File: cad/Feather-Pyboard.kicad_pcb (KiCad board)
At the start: 2 copper layers, 22.9 x 55.9 mm, 39 parts, among them P1 CONN_01X16, P2 CONN_01X02, P3 CONN_01X12, P4 USB_OTG, SW1 RST, U1 SPX3819, U2 MCP73811T-420I/OT, U3 STM32F411CEUx, U4 MicroSD_SPI_CD, Y1 32.768Hz, Y2 8MHz

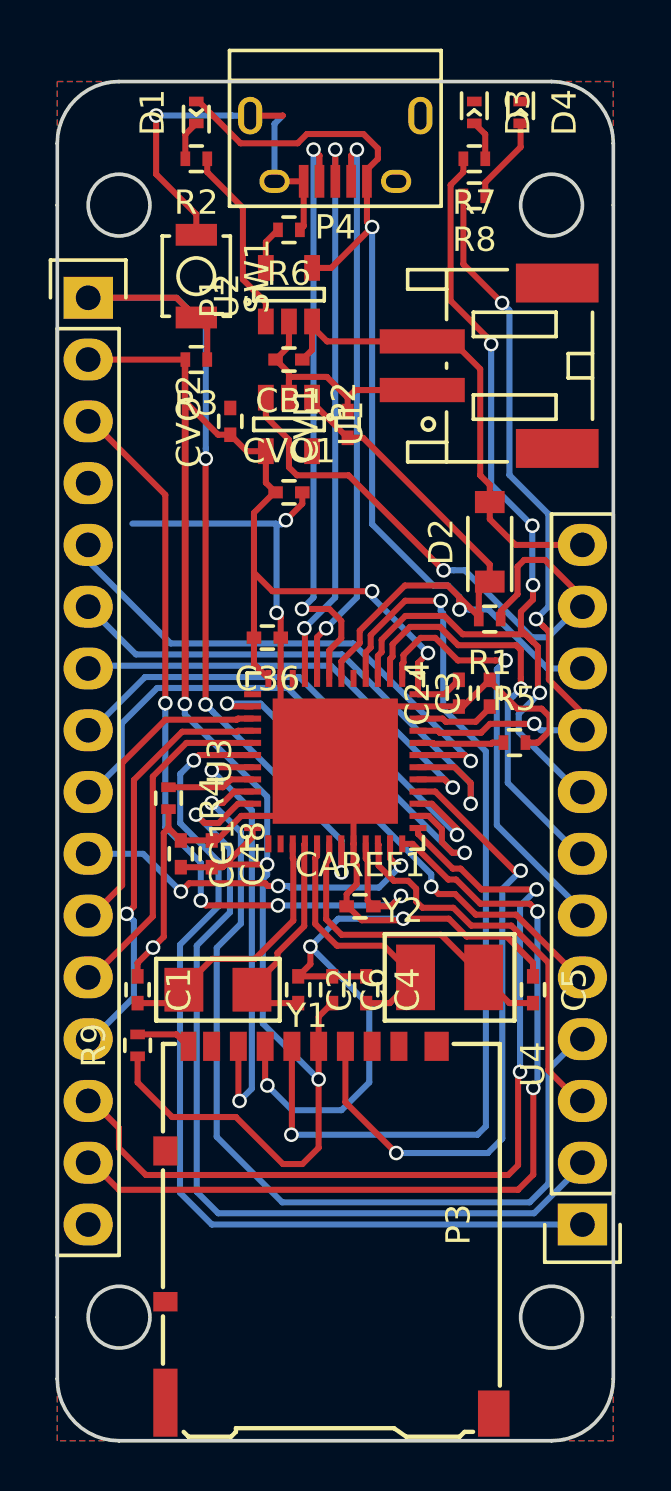
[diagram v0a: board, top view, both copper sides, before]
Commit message: new crystal footrpints and 22 ohm resistors for usb
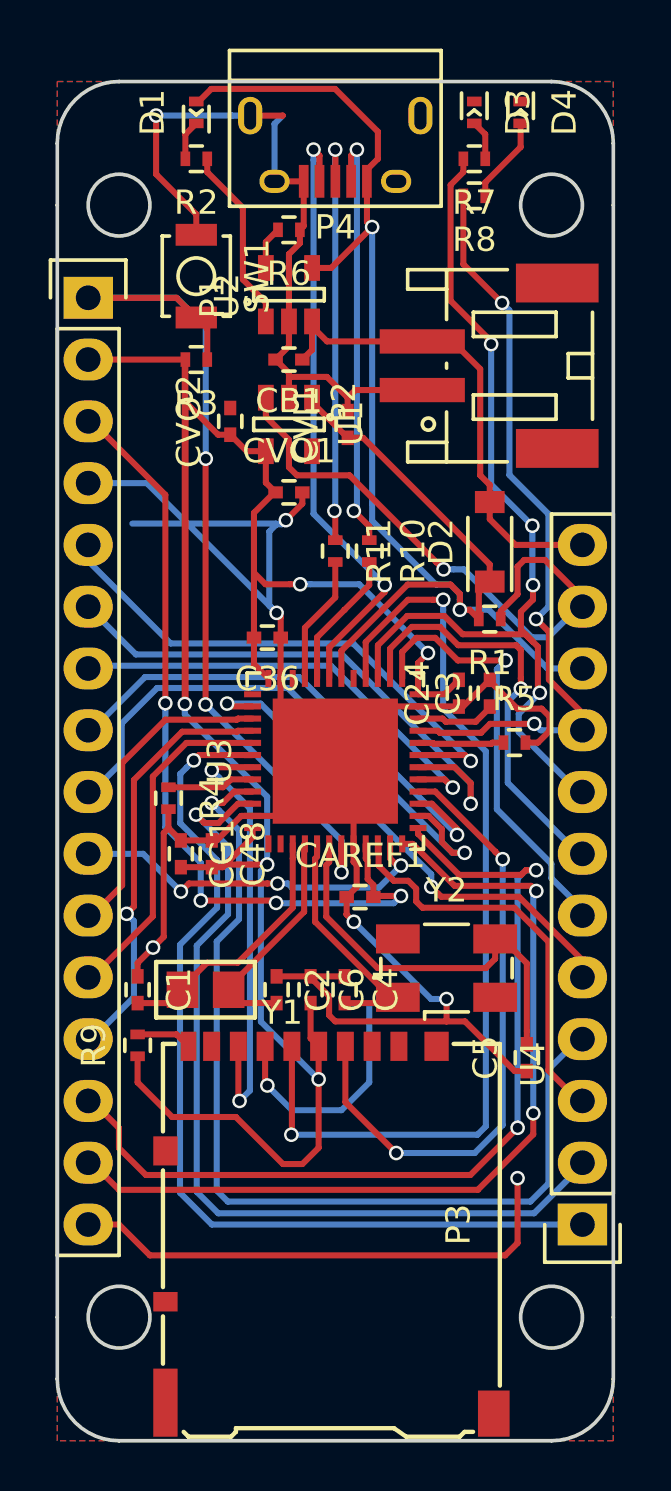
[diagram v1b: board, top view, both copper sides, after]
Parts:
- added R10: 22, Resistors_SMD:R_0402, F.Cu at (150.0, 77.7)
- added R11: 22, Resistors_SMD:R_0402, F.Cu at (148.6, 77.7)
- Y1: footprint smt:R-1206 -> smt:R-0805
- Y2: footprint smt:R-1210 -> Crystals:Crystal_SMD_ABM3B
- moved C5 2.81 mm to (156.5, 98.6), turned to 90 degrees
- moved C2 0.89 mm to (146.2, 95.8)
- moved C4 0.89 mm to (149.0, 95.8)
- moved C6 0.89 mm to (147.6, 95.8)
- moved Y1 0.51 mm to (143.3, 95.8)
- moved Y2 0.40 mm to (153.2, 94.9)
- moved CAREF1 0.38 mm to (149.6, 91.9)
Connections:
- U3 pad 32: Net-(P4-Pad2) -> Net-(R10-Pad2)
- U3 pad 33: Net-(P4-Pad3) -> Net-(R11-Pad2)
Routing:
- net GND: track 102.3 -> 136.9 mm, vias 7 -> 8
- net Net-(P4-Pad3): track 23.6 -> 17.4 mm
- net Net-(P4-Pad2): track 23.8 -> 17.8 mm
- net Net-(R10-Pad2): track 0.00 -> 5.68 mm
- net OSCOUT: track 13.1 -> 18.4 mm
- net Net-(R11-Pad2): track 0.00 -> 5.30 mm
- net IO5: track 38.2 -> 39.4 mm
- net DI: track 26.8 -> 25.7 mm
- net AREF: track 34.2 -> 33.6 mm
- net OSCIN: track 10.8 -> 10.2 mm
- net TX: track 36.6 -> 36.1 mm
- net IO6: track 16.2 -> 16.7 mm
- net OSC32OUT: track 9.03 -> 9.53 mm
